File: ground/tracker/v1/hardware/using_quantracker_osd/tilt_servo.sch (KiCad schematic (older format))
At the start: 16 parts, among them K3 CONN_3, U1 SMPSU_module, U2 SI8610, U3 MIC5205

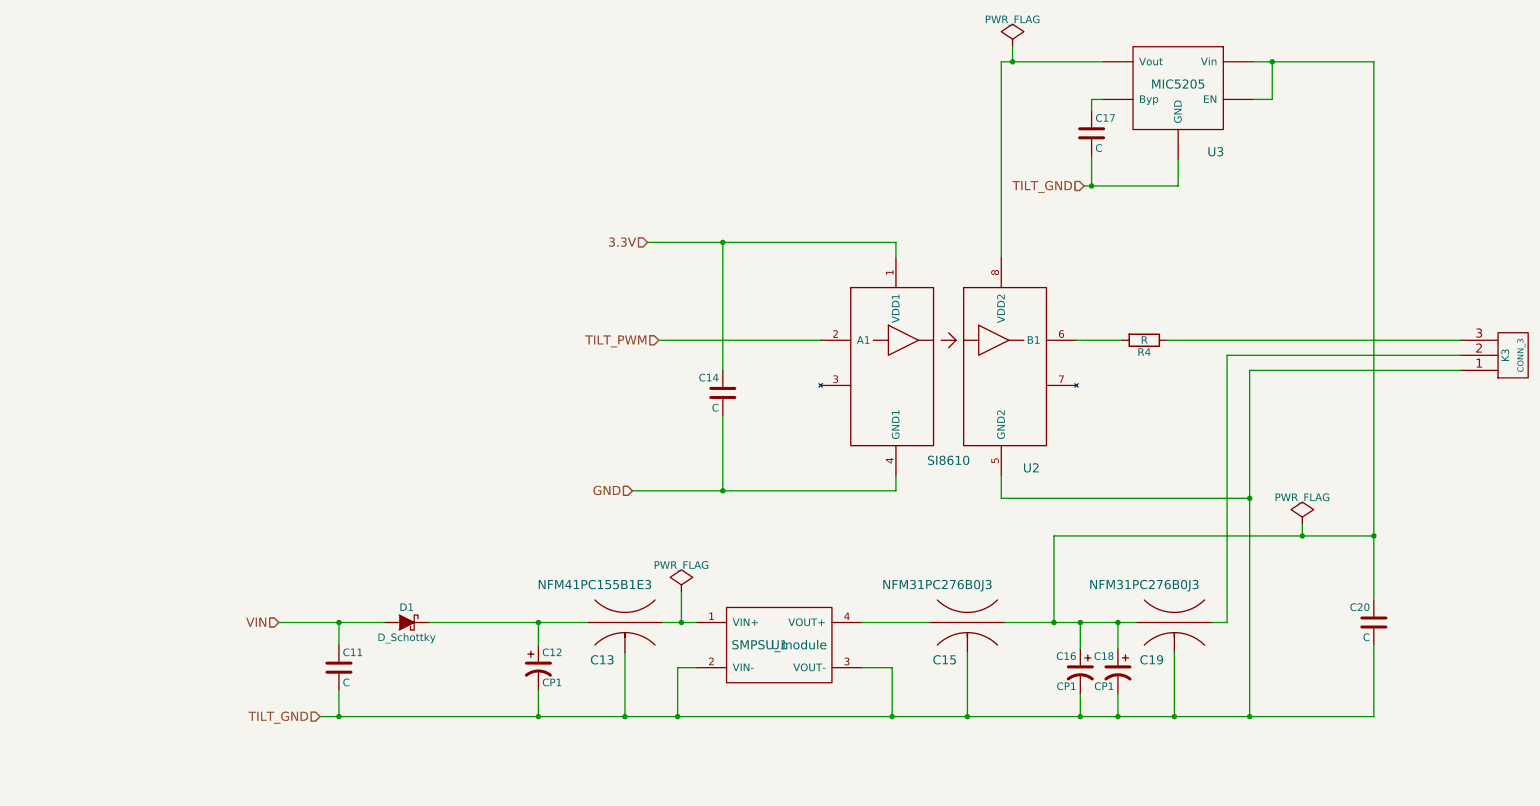
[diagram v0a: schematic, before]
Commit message: add i2c and gps connectors
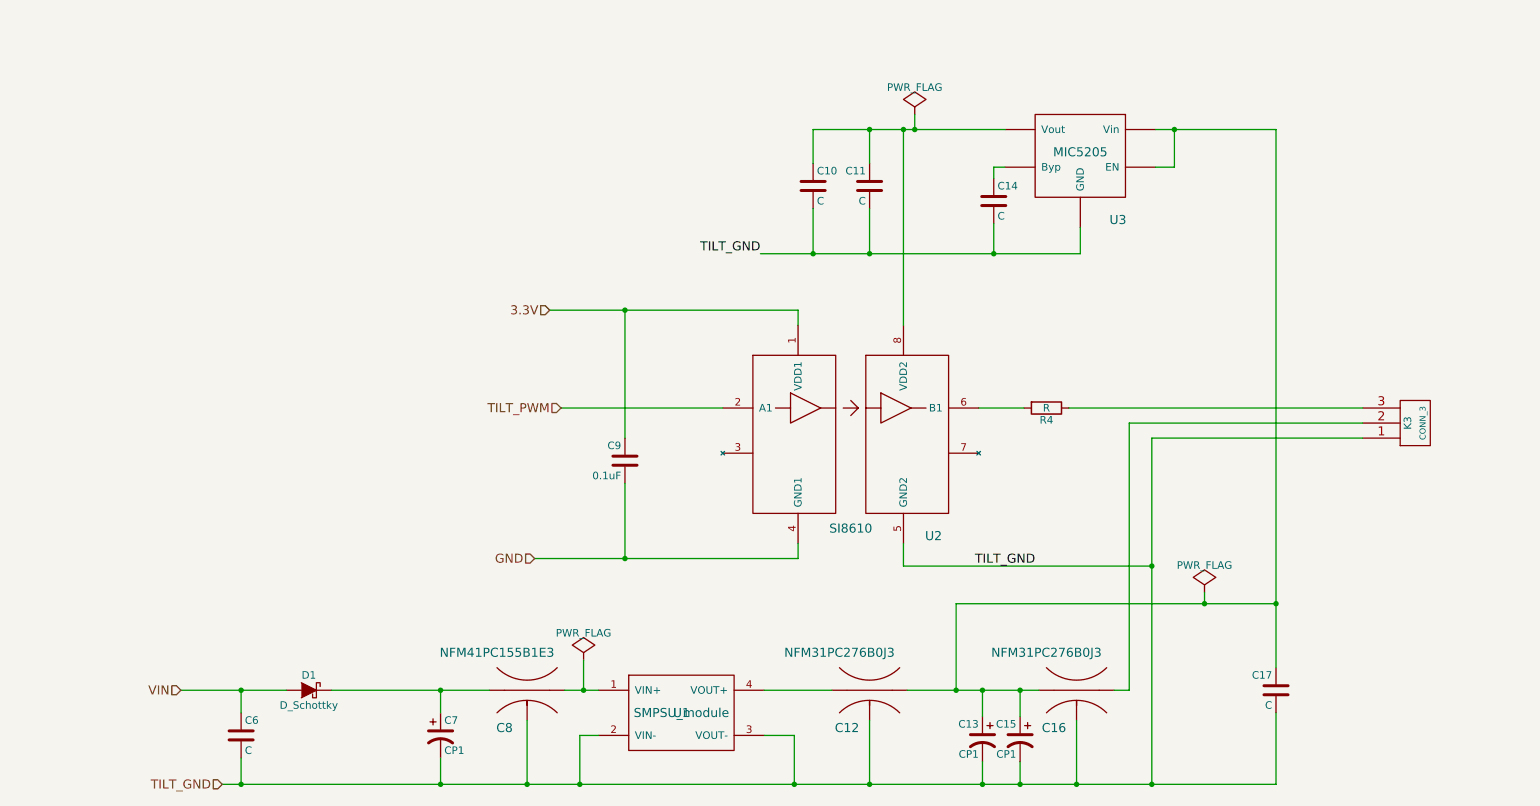
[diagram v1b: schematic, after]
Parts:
- added C10, C11: C, symbol C
- C9: renamed from C14; value C -> 0.1uF
- renumbered C15 to C12, C16 to C13, C17 to C14, C18 to C15, C19 to C16, C20 to C17, C11 to C6, C12 to C7, C13 to C8
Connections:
- net TILT_GND: now also C10.2, C11.2
- net at U2.8 (VDD2), U3.~ (Vout): now also C10.1, C11.1
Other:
- moved on the sheet: C12, C13, C14, C15, C16, C17, C6, C7, C8, C9, D1, K3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

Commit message: move encoder up out of pan motor schematic
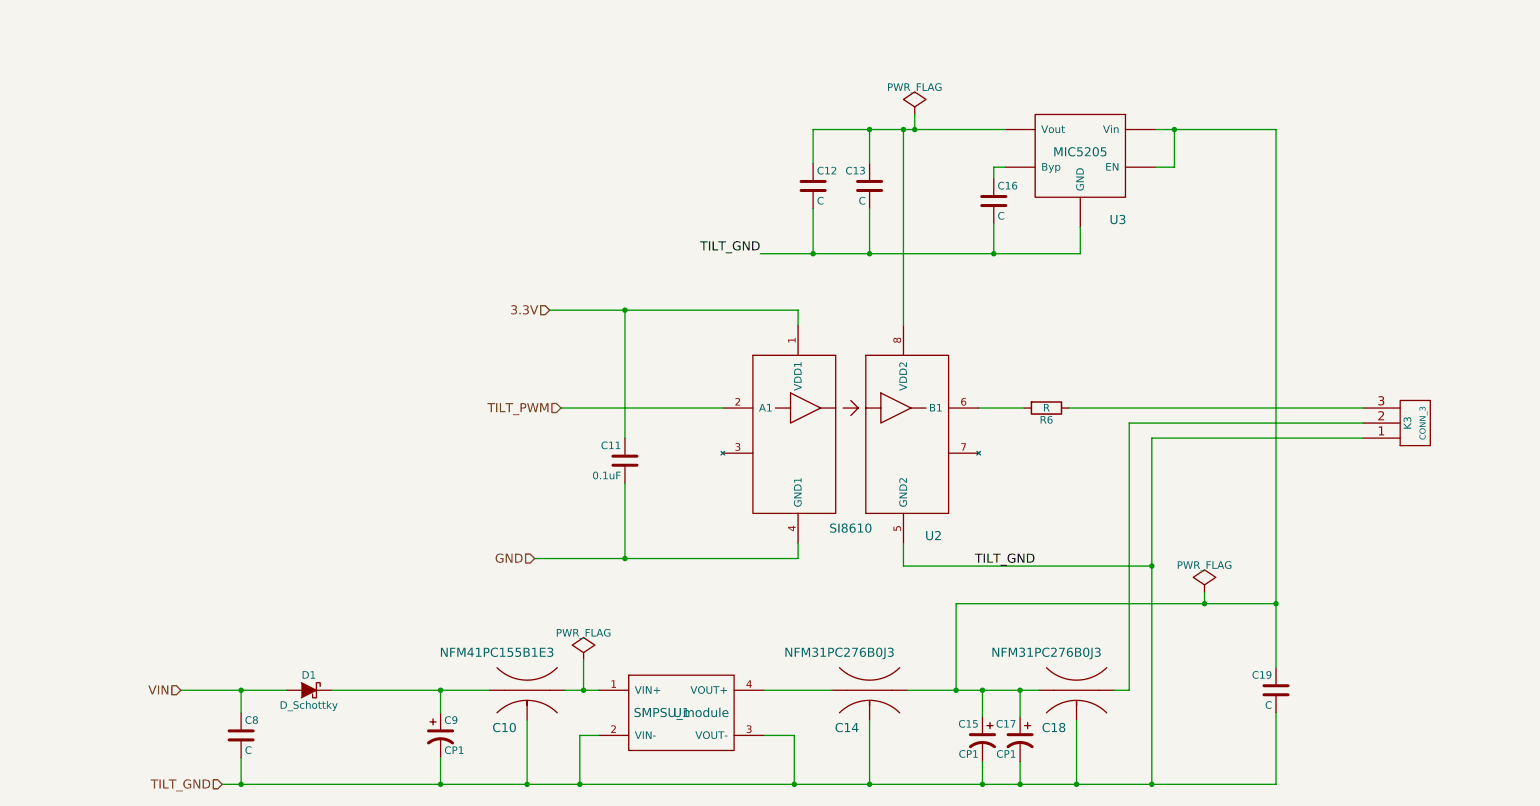
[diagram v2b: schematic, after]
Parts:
- renumbered C8 to C10, C9 to C11, C10 to C12, C11 to C13, C12 to C14, C13 to C15, C14 to C16, C15 to C17, C16 to C18, C17 to C19, C6 to C8, C7 to C9, R4 to R6
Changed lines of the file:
@@
 	5975 5250 5525 5250
 $Comp
-L CAP3T C8
+L CAP3T C10
 U 1 1 587F5406
 P 3950 5250
-F 0 "C8" H 4100 5000 60  0000 C CNN
+F 0 "C10" H 4100 5000 60  0000 C CNN
 F 1 "NFM41PC155B1E3" H 4150 5500 60  0000 C CNN
 F 2 "" H 3950 5250 60  0001 C CNN
@@
 $EndComp
 $Comp
-L CAP3T C16
+L CAP3T C18
 U 1 1 587F540D
 P 7600 5250
-F 0 "C16" H 7750 5000 60  0000 C CNN
+F 0 "C18" H 7750 5000 60  0000 C CNN
 F 1 "NFM31PC276B0J3" H 7800 5500 60  0000 C CNN
 F 2 "" H 7600 5250 60  0001 C CNN
@@
 	4300 5875 4300 5550
 $Comp
-L C C9
+L C C11
 U 1 1 587F6489
 P 4600 3725
-F 0 "C9" H 4625 3825 50  0000 L CNN
+F 0 "C11" H 4625 3825 50  0000 L CNN
 F 1 "0.1uF" H 4625 3625 50  0000 L CNN
 F 2 "" H 4638 3575 50  0000 C CNN
@@
 Connection ~ 4600 4375
 $Comp
-L CP1 C13
+L CP1 C15
 U 1 1 587F671D
 P 6975 5575
-F 0 "C13" H 7000 5675 50  0000 L CNN
+F 0 "C15" H 7000 5675 50  0000 L CNN
 F 1 "CP1" H 7000 5475 50  0000 L CNN
 F 2 "" H 6975 5575 50  0000 C CNN
@@
 Connection ~ 6975 5875
 $Comp
-L CAP3T C12
+L CAP3T C14
 U 1 1 587F6F9B
 P 6225 5250
-F 0 "C12" H 6375 5000 60  0000 C CNN
+F 0 "C14" H 6375 5000 60  0000 C CNN
 F 1 "NFM31PC276B0J3" H 6425 5500 60  0000 C CNN
 F 2 "" H 6225 5250 60  0001 C CNN
@@
 Connection ~ 6225 5875
 $Comp
-L C C17
+L C C19
 U 1 1 587F7305
 P 8925 5250
-F 0 "C17" H 8950 5350 50  0000 L CNN
+F 0 "C19" H 8950 5350 50  0000 L CNN
 F 1 "C" H 8950 5150 50  0000 L CNN
 F 2 "" H 8963 5100 50  0000 C CNN
@@
 	4175 3375 5250 3375
 $Comp
-L CP1 C7
+L CP1 C9
 U 1 1 587FA8DB
 P 3375 5550
-F 0 "C7" H 3400 5650 50  0000 L CNN
+F 0 "C9" H 3400 5650 50  0000 L CNN
 F 1 "CP1" H 3400 5450 50  0000 L CNN
 F 2 "" H 3375 5550 50  0000 C CNN
@@
 Connection ~ 3375 5875
 $Comp
-L C C6
+L C C8
 U 1 1 58802A97
 P 2050 5550
-F 0 "C6" H 2075 5650 50  0000 L CNN
+F 0 "C8" H 2075 5650 50  0000 L CNN
 F 1 "C" H 2075 5450 50  0000 L CNN
 F 2 "" H 2088 5400 50  0000 C CNN
@@
 Connection ~ 2050 5875
 $Comp
-L CP1 C15
+L CP1 C17
 U 1 1 587FC59F
 P 7225 5575
-F 0 "C15" H 7250 5675 50  0000 L CNN
+F 0 "C17" H 7250 5675 50  0000 L CNN
 F 1 "CP1" H 7250 5475 50  0000 L CNN
 F 2 "" H 7225 5575 50  0000 C CNN
@@
 Connection ~ 8250 1525
 $Comp
-L C C14
+L C C16
 U 1 1 5880CEC7
 P 7050 2000
-F 0 "C14" H 7075 2100 50  0000 L CNN
+F 0 "C16" H 7075 2100 50  0000 L CNN
 F 1 "C" H 7075 1900 50  0000 L CNN
 F 2 "" H 7088 1850 50  0000 C CNN
@@
 Connection ~ 7050 2350
 $Comp
-L R R4
+L R R6
 U 1 1 5880DDCF
 P 7400 3375
-F 0 "R4" V 7480 3375 50  0000 C CNN
+F 0 "R6" V 7480 3375 50  0000 C CNN
 F 1 "R" V 7400 3375 50  0000 C CNN
 F 2 "" V 7330 3375 50  0000 C CNN
@@
 $EndComp
 $Comp
-L PWR_FLAG #FLG07
+L PWR_FLAG #FLG09
 U 1 1 5881F289
 P 6525 1425
-F 0 "#FLG07" H 6525 1520 50  0001 C CNN
+F 0 "#FLG09" H 6525 1520 50  0001 C CNN
 F 1 "PWR_FLAG" H 6525 1605 50  0000 C CNN
 F 2 "" H 6525 1425 50  0000 C CNN
@@
 $EndComp
 $Comp
-L PWR_FLAG #FLG08
+L PWR_FLAG #FLG010
 U 1 1 5881F33B
 P 8450 4600
-F 0 "#FLG08" H 8450 4695 50  0001 C CNN
+F 0 "#FLG010" H 8450 4695 50  0001 C CNN
 F 1 "PWR_FLAG" H 8450 4780 50  0000 C CNN
 F 2 "" H 8450 4600 50  0000 C CNN
@@
 Connection ~ 6525 1525
 $Comp
-L PWR_FLAG #FLG09
+L PWR_FLAG #FLG011
 U 1 1 5881F699
 P 4325 5050
-F 0 "#FLG09" H 4325 5145 50  0001 C CNN
+F 0 "#FLG011" H 4325 5145 50  0001 C CNN
 F 1 "PWR_FLAG" H 4325 5230 50  0000 C CNN
 F 2 "" H 4325 5050 50  0000 C CNN
@@
 Connection ~ 4325 5250
 $Comp
-L C C11
+L C C13
 U 1 1 588213ED
 P 6225 1900
-F 0 "C11" H 6250 2000 50  0000 L CNN
+F 0 "C13" H 6250 2000 50  0000 L CNN
 F 1 "C" H 6250 1800 50  0000 L CNN
 F 2 "" H 6263 1750 50  0000 C CNN
@@
 	6225 2350 6225 2050
 $Comp
-L C C10
+L C C12
 U 1 1 5882181F
 P 5850 1900
-F 0 "C10" H 5875 2000 50  0000 L CNN
+F 0 "C12" H 5875 2000 50  0000 L CNN
 F 1 "C" H 5875 1800 50  0000 L CNN
 F 2 "" H 5888 1750 50  0000 C CNN

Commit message: remove isolator frm pan motor
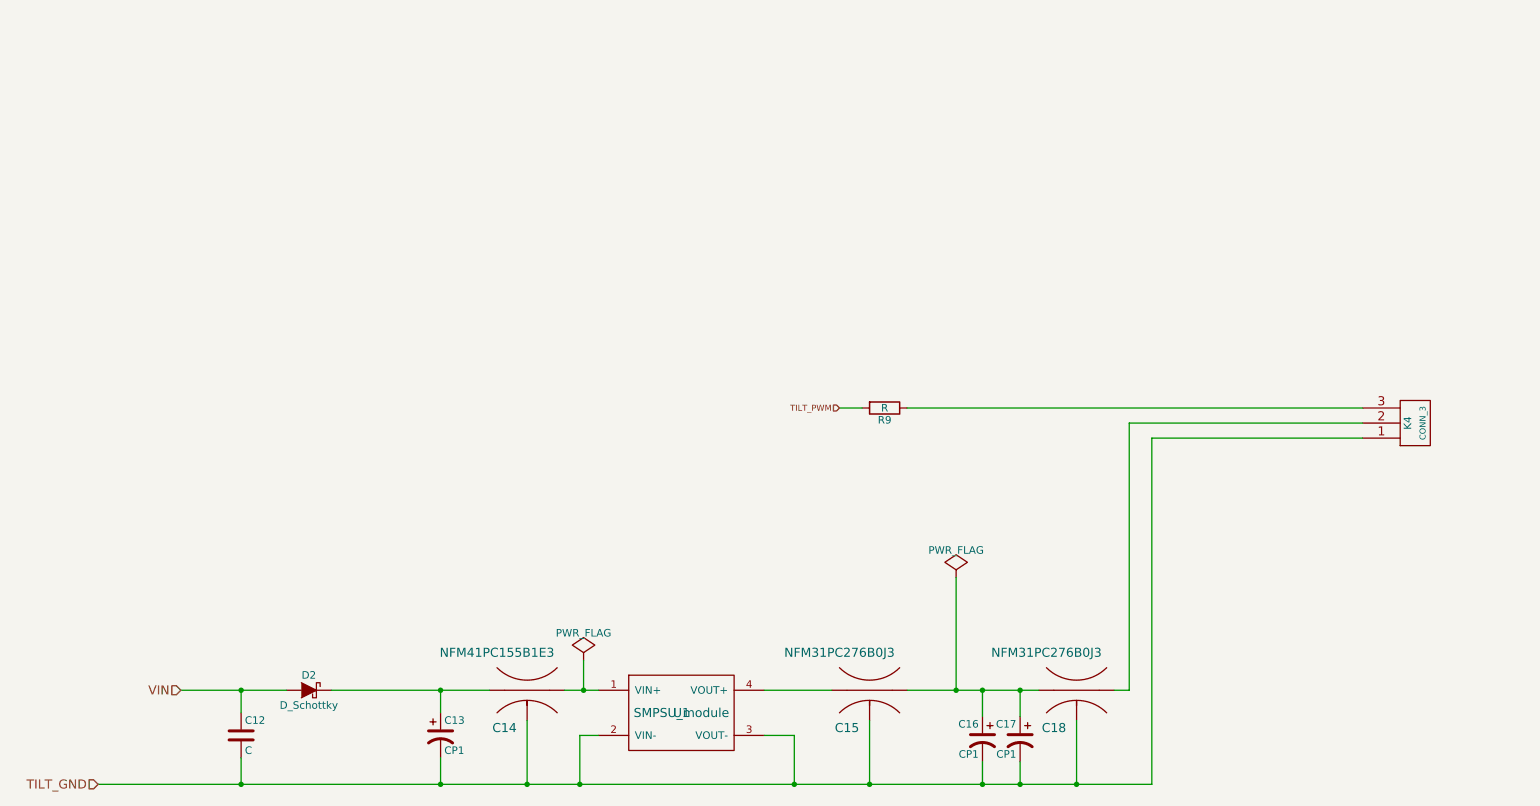
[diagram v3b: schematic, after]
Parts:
- removed C11: 0.1uF, symbol C
- removed C12, C13, C16, C19: C, symbol C
- removed R6: R, symbol R
- removed U2: SI8610, symbol SI8610
- removed U3: MIC5205, symbol MIC5205
- added R9: R, symbol R
- renumbered C8 to C12, C9 to C13, C10 to C14, C14 to C15, C15 to C16, D1 to D2, K3 to K4
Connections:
- net TILT_PWM: now also R9.2
- net at K4.3 (P3): now also R9.1
